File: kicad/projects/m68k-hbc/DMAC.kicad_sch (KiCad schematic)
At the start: 16 parts, among them U1 74LS04, U2 74LS245, U3 74LS573, U4 MC68440FN, U5 74LS245, U6 74LS245, U7 74LS573, X5 10M

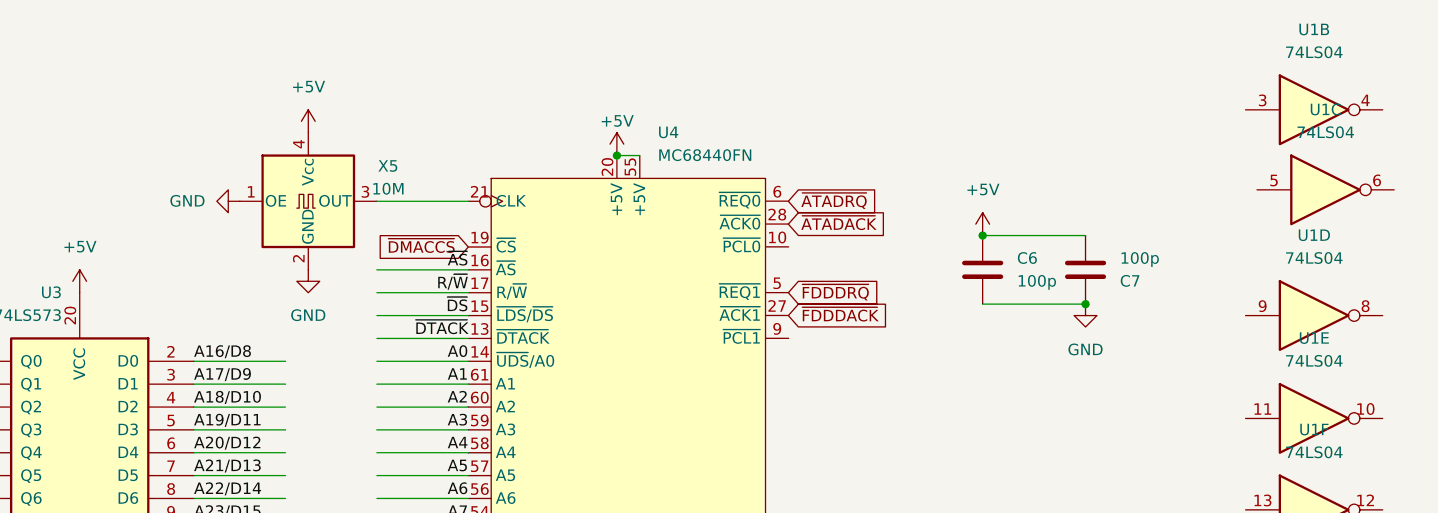
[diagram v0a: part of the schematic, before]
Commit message: Modified system architecture, New KiCad Project: Cache Memory Module(SIMM80)
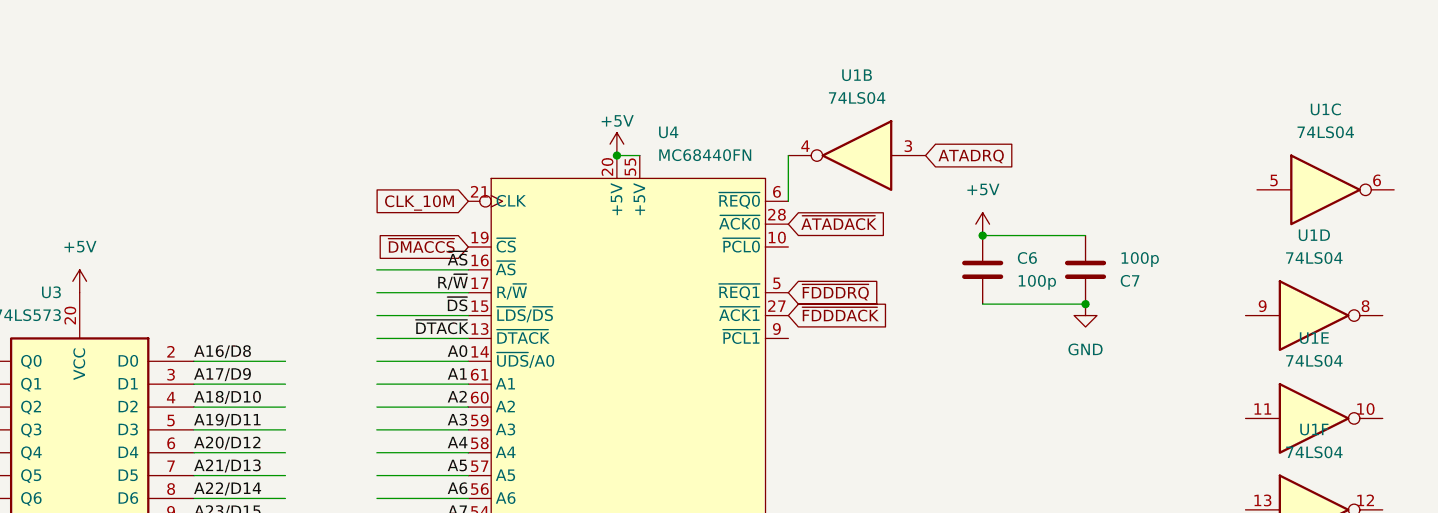
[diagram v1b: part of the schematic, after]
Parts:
- removed X5: 10M, Oscillator:Oscillator_SMD_SeikoEpson_SG8002CA-4Pin_7.0x5.0mm, symbol Oscillator:SG-8002CA
- U4: symbol MC68440FN:MC68440FN -> m68k-hbc-ic:MC68440FN
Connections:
- net ~{ATADACK}: now also U4.28 (~{ACK0})
- net ~{FDDDACK}: now also U4.27 (~{ACK1})
- net ~{FDDDRQ}: now also U4.5 (~{REQ1})
- net ATADRQ: now reaches U1.3
- net at U1.4: now also U4.6 (~{REQ0})
- net CLK_10M: now reaches U4.21 (CLK)
